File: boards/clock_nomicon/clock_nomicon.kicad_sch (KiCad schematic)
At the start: 24 parts, among them J1 USB-MicroB-power, J2 Conn_01x06, SW1 SW_speed_sel, SW2 SW_clock_sel, SW3 SW_clock, SW4 SW_reset, U1 74HC14

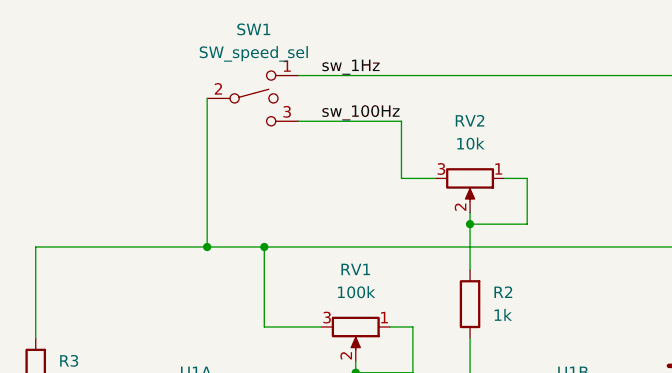
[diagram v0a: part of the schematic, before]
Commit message: clock_nomicon: add board design
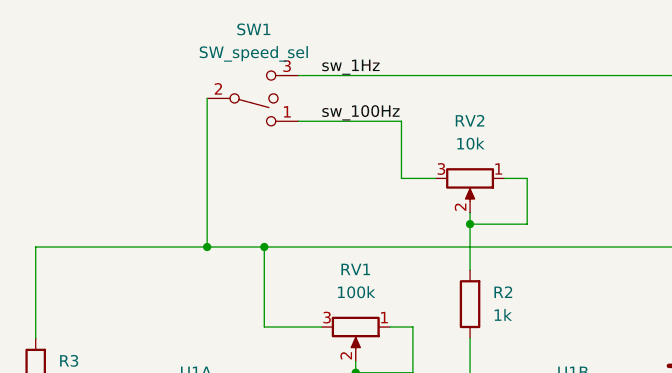
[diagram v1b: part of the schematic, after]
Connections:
- net sw_100Hz: now also SW1.1; no longer SW1.3
- net sw_1Hz: now also SW1.3; no longer SW1.1
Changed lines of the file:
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@@
     (pin "1")
   )
-  (symbol (lib_id "Switch:SW_SPDT_MSM") (at 76.2 35.56 0) (unit 1)
+  (symbol (lib_id "Switch:SW_SPDT_MSM") (at 76.2 35.56 0) (mirror x) (unit 1)
     (in_bom yes) (on_board yes) (fields_autoplaced)
     (property "Reference" "SW1" (id 0) (at 76.327 27.94 0))
